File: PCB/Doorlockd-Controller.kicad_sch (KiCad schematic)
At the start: 58 parts, among them J10 Power Out 1, J11 DC in, J12 GPIO 3, J13 Debug UART, J14 GPIO 4, J15 Power Out 2, J16 to extra screw conn., J18 GPIO only MilkV 1.8V, J19 3V 5V Vin, J20 3V 5V Vin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

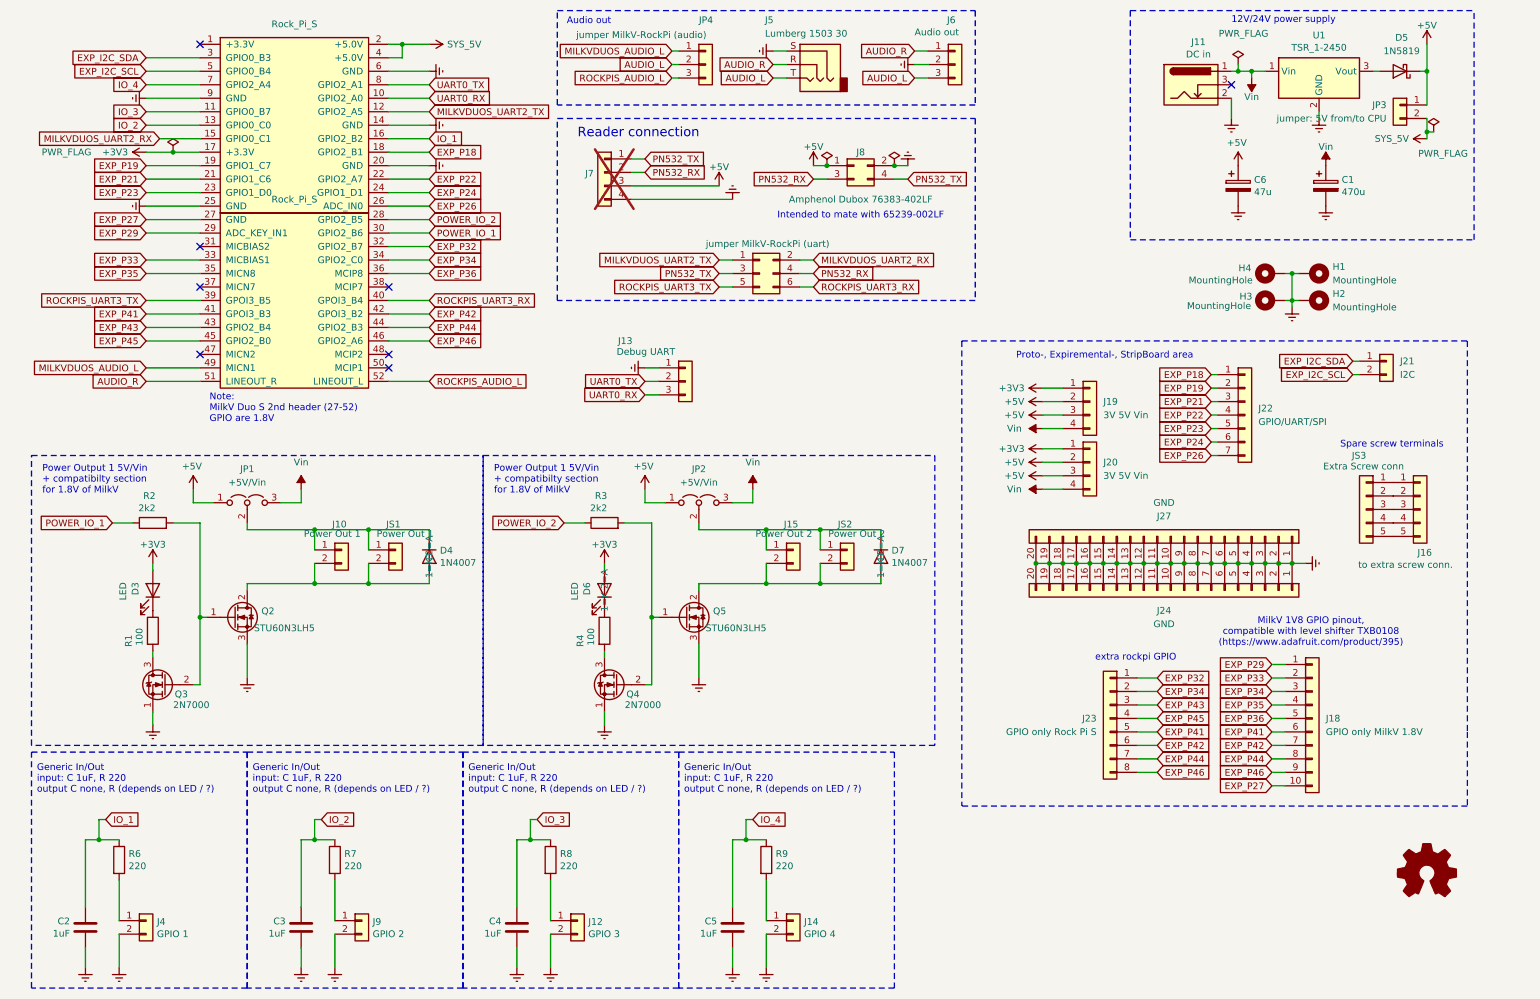
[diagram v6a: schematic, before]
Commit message: Fixed and improved spreadsheet, pcb and schema
PCB and Schema:
improved netlabels for PN532 related pins.
improved netlabels for OUT_1 / OUT_2
improved netlabels for EXP P03 / EXP P05 , and fixed copper lines accoording to silkscreen labels.
added 3.3V pin on PCB intended for lelvel shifter Milk V DUO S (EXP_P43)
Added help lines for mountingholes on fab layer.
Fixed mounting holes for 120x90 & 118x91 including correct positioning.

Spreadsheet:
Fixed and improved color and text labels.
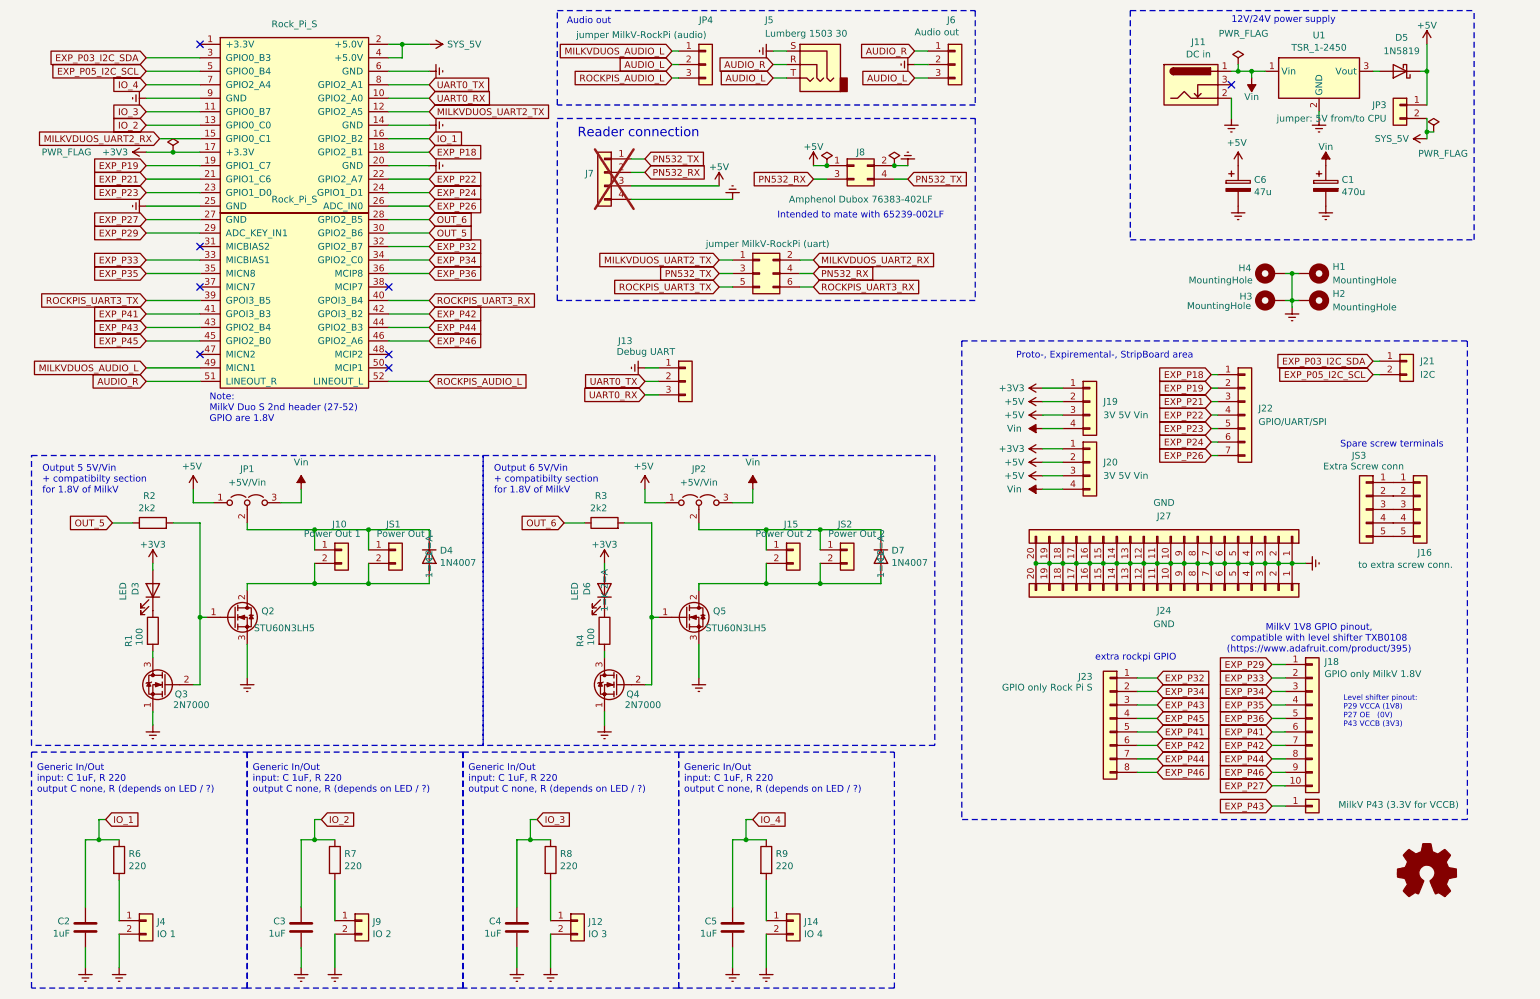
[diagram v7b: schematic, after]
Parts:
- added J1: MilkV P43 (3.3V for VCCB), StripBoard:StripBoard_1x01_P2.54mm, symbol Connector_Generic:Conn_01x01
- H1: footprint MountingHole_3.2x4.32mm_Oval_22.5deg:MountingHole_3.2x4.32mm_Oval_22.5deg_Rtop -> MountingHole_3.2x4.32mm_Oval_22.5deg:MountingHole_3.2x4.32mm_Oval_22.5deg
- H2: footprint MountingHole_3.2x4.32mm_Oval_22.5deg:MountingHole_3.2x4.32mm_Oval_22.5deg_Rbottom -> MountingHole_3.2x4.32mm_Oval_22.5deg:MountingHole_3.2x4.32mm_Oval_22.5deg
- H3: footprint MountingHole_3.2x4.32mm_Oval_22.5deg:MountingHole_3.2x4.32mm_Oval_22.5deg_Lbottom -> MountingHole_3.2x4.32mm_Oval_22.5deg:MountingHole_3.2x4.32mm_Oval_22.5deg
- H4: footprint MountingHole_3.2x4.32mm_Oval_22.5deg:MountingHole_3.2x4.32mm_Oval_22.5deg_Ltop -> MountingHole_3.2x4.32mm_Oval_22.5deg:MountingHole_3.2x4.32mm_Oval_22.5deg
- J12: value GPIO 3 -> IO 3
- J14: value GPIO 4 -> IO 4
- J4: value GPIO 1 -> IO 1
- J9: value GPIO 2 -> IO 2
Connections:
- net EXP_P43: now also J1.1 (Pin_1)
- net EXP_I2C_SCL renamed EXP_P05_I2C_SCL
- net EXP_I2C_SDA renamed EXP_P03_I2C_SDA
- net POWER_IO_1 renamed OUT_5
- net POWER_IO_2 renamed OUT_6
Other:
- note added: "Level shifter pinout: P29 VCCA (1V8) P27 OE (0V) P43 VCCB (3V3)"
- note added: "Output 5 5V/Vin + compatibilty section for 1.8V of MilkV"
- note added: "Output 6 5V/Vin + compatibilty section for 1.8V of MilkV"
- note removed: "Power Output 1 5V/Vin + compatibilty section for 1.8V of MilkV"
- moved on the sheet: J21
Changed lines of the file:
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@@
 		)
 	)
-	(text "Power Output 1 5V/Vin\n+ compatibilty section \nfor 1.8V of MilkV "
+	(text "Output 6 5V/Vin\n+ compatibilty section \nfor 1.8V of MilkV "
 		(exclude_from_sim no)
 		(at 99.822 103.886 0)
@@
 	(text "MilkV 1V8 GPIO pinout, \ncompatible with level shifter TXB0108 \n(https://www.adafruit.com/product/395)"
 		(exclude_from_sim no)
-		(at 253.746 129.794 0)
+		(at 255.27 131.064 0)
 		(effects
 			(font
@@
 		)
 	)
-	(text "Power Output 1 5V/Vin\n+ compatibilty section \nfor 1.8V of MilkV "
+	(text "Output 5 5V/Vin\n+ compatibilty section \nfor 1.8V of MilkV "
 		(exclude_from_sim no)
 		(at 14.732 103.886 0)
@@
 		)
 	)
+	(text "Level shifter pinout:\nP29 VCCA (1V8)\nP27 OE   (0V)\nP43 VCCB (3V3)"
+		(exclude_from_sim no)
+		(at 259.842 144.78 0)
+		(effects
+			(font
+				(size 1.016 1.016)
+			)
+			(justify left)
+		)
+	)
 	(text "Proto-, Expiremental-, StripBoard area\n"
 		(exclude_from_sim no)
@@
 	(polyline
 		(pts
-			(xy 283.21 162.56) (xy 187.96 162.56)
+			(xy 283.21 165.1) (xy 187.96 165.1)
 		)
 		(stroke
@@
 	(wire
 		(pts
-			(xy 261.62 81.28) (xy 262.89 81.28)
+			(xy 265.43 81.28) (xy 266.7 81.28)
 		)
 		(stroke
@@
 	(polyline
 		(pts
-			(xy 283.21 148.59) (xy 283.21 162.56)
+			(xy 283.21 148.59) (xy 283.21 165.1)
 		)
 		(stroke
@@
 	(wire
 		(pts
+			(xy 246.38 162.56) (xy 248.92 162.56)
+		)
+		(stroke
+			(width 0)
+			(type default)
+		)
+	)
+	(wire
+		(pts
 			(xy 132.08 105.41) (xy 128.27 105.41)
 		)
@@
 	(wire
 		(pts
-			(xy 261.62 78.74) (xy 262.89 78.74)
+			(xy 265.43 78.74) (xy 266.7 78.74)
 		)
 		(stroke
@@
 	(polyline
 		(pts
-			(xy 187.96 74.93) (xy 187.96 162.56)
+			(xy 187.96 74.93) (xy 187.96 165.1)
 		)
 		(stroke
@@
 		)
 	)
-	(global_label "POWER_IO_1"
+	(global_label "OUT_5"
 		(shape input)
 		(at 87.63 54.61 0)
@@
 		)
 		(property "Intersheetrefs" "${INTERSHEET_REFS}"
-			(at 101.5119 54.61 0)
+			(at 95.7667 54.61 0)
 			(effects
 				(font
@@
 		)
 	)
-	(global_label "EXP_I2C_SCL"
+	(global_label "EXP_P43"
+		(shape input)
+		(at 246.38 162.56 180)
+		(fields_autoplaced yes)
+		(effects
+			(font
+				(size 1.27 1.27)
+			)
+			(justify right)
+		)
+		(property "Intersheetrefs" "${INTERSHEET_REFS}"
+			(at 235.7639 162.56 0)
+			(effects
+				(font
+					(size 1.27 1.27)
+				)
+				(justify right)
+				(hide yes)
+			)
+		)
+	)
+	(global_label "EXP_P05_I2C_SCL"
 		(shape input)
 		(at 34.29 24.13 180)
@@
 		)
 		(property "Intersheetrefs" "${INTERSHEET_REFS}"
-			(at 19.8034 24.13 0)
+			(at 15.1468 24.13 0)
 			(effects
 				(font
@@
 		)
 	)
-	(global_label "EXP_I2C_SDA"
+	(global_label "EXP_P03_I2C_SDA"
 		(shape input)
 		(at 34.29 21.59 180)
@@
 		)
 		(property "Intersheetrefs" "${INTERSHEET_REFS}"
-			(at 19.7429 21.59 0)
+			(at 15.0863 21.59 0)
 			(effects
 				(font
@@
 		)
 	)
-	(global_label "POWER_IO_1"
+	(global_label "OUT_5"
 		(shape input)
 		(at 27.94 109.22 180)
@@
 		)
 		(property "Intersheetrefs" "${INTERSHEET_REFS}"
-			(at 14.0581 109.22 0)
+			(at 19.8033 109.22 0)
 			(effects
 				(font
@@
 		)
 	)
-	(global_label "POWER_IO_2"
+	(global_label "OUT_6"
 		(shape input)
 		(at 87.63 52.07 0)
@@
 		)
 		(property "Intersheetrefs" "${INTERSHEET_REFS}"
-			(at 101.5119 52.07 0)
+			(at 95.7667 52.07 0)
 			(effects
 				(font
@@
 		)
 	)
-	(global_label "EXP_I2C_SDA"
+	(global_label "EXP_P03_I2C_SDA"
 		(shape input)
-		(at 261.62 78.74 180)
+		(at 265.43 78.74 180)
 		(fields_autoplaced yes)
 		(effects
@@
 		)
 		(property "Intersheetrefs" "${INTERSHEET_REFS}"
-			(at 247.0729 78.74 0)
+			(at 246.2263 78.74 0)
 			(effects
 				(font
@@
 		)
 	)
-	(global_label "EXP_I2C_SCL"
+	(global_label "EXP_P05_I2C_SCL"
 		(shape input)
-		(at 261.62 81.28 180)
+		(at 265.43 81.28 180)
 		(fields_autoplaced yes)
 		(effects
@@
 		)
 		(property "Intersheetrefs" "${INTERSHEET_REFS}"
-			(at 247.1334 81.28 0)
+			(at 246.2868 81.28 0)
 			(effects
 				(font
@@
 		)
 	)
-	(global_label "POWER_IO_2"
+	(global_label "OUT_6"
 		(shape input)
 		(at 113.03 109.22 180)
@@
 		)
 		(property "Intersheetrefs" "${INTERSHEET_REFS}"
-			(at 99.1481 109.22 0)
+			(at 104.8933 109.22 0)
 			(effects
 				(font
@@
 			)
 		)
-		(property "Value" "GPIO 1"
+		(property "Value" "IO 1"
 			(at 36.322 186.6646 0)
 			(effects
@@
 			)
 		)
-		(property "Footprint" "MountingHole_3.2x4.32mm_Oval_22.5deg:MountingHole_3.2x4.32mm_Oval_22.5deg_Rbottom"
+		(property "Footprint" "MountingHole_3.2x4.32mm_Oval_22.5deg:MountingHole_3.2x4.32mm_Oval_22.5deg"
 			(at 254 67.31 0)
 			(effects
@@
 	(symbol
 		(lib_id "Connector_Generic:Conn_01x02")
-		(at 267.97 78.74 0)
+		(at 271.78 78.74 0)
 		(unit 1)
 		(exclude_from_sim no)
@@
 		(fields_autoplaced yes)
 		(property "Reference" "J21"
-			(at 270.51 78.7399 0)
+			(at 274.32 78.7399 0)
 			(effects
 				(font
@@
 		)
 		(property "Value" "I2C"
-			(at 270.51 81.2799 0)
+			(at 274.32 81.2799 0)
 			(effects
 				(font
@@
 		)
 		(property "Footprint" "StripBoard:StripBoard_1x02_P2.54mm"
-			(at 267.97 78.74 0)
+			(at 271.78 78.74 0)
 			(effects
 				(font
@@
 		)
 		(property "Datasheet" "~"
-			(at 267.97 78.74 0)
+			(at 271.78 78.74 0)
 			(effects
 				(font
@@
 		)
 		(property "Description" "Generic connector, single row, 01x02, script generated (kicad-library-utils/schlib/autogen/connector/)"
-			(at 267.97 78.74 0)
+			(at 271.78 78.74 0)
 			(effects
 				(font
@@
 			)
 		)
-		(property "Footprint" "MountingHole_3.2x4.32mm_Oval_22.5deg:MountingHole_3.2x4.32mm_Oval_22.5deg_Lbottom"
+		(property "Footprint" "MountingHole_3.2x4.32mm_Oval_22.5deg:MountingHole_3.2x4.32mm_Oval_22.5deg"
 			(at 246.38 67.31 0)
 			(effects
@@
 			)
 		)
-		(property "Footprint" "MountingHole_3.2x4.32mm_Oval_22.5deg:MountingHole_3.2x4.32mm_Oval_22.5deg_Ltop"
+		(property "Footprint" "MountingHole_3.2x4.32mm_Oval_22.5deg:MountingHole_3.2x4.32mm_Oval_22.5deg"
 			(at 246.38 62.23 0)
 			(effects
@@
 		(dnp no)
 		(property "Reference" "J23"
-			(at 213.36 146.0499 0)
+			(at 212.598 138.176 0)
 			(effects
 				(font
@@
 		)
 		(property "Value" "GPIO only Rock Pi S"
-			(at 213.36 148.5899 0)
+			(at 212.598 140.208 0)
 			(effects
 				(font
@@
 		(dnp no)
 		(property "Reference" "J18"
-			(at 256.54 146.0499 0)
+			(at 256.286 135.382 0)
 			(effects
 				(font
@@
 		)
 		(property "Value" "GPIO only MilkV 1.8V"
-			(at 256.54 148.5899 0)
+			(at 256.286 137.668 0)
 			(effects
 				(font
@@
 			)
 		)
-		(property "Value" "GPIO 3"
+		(property "Value" "IO 3"
 			(at 117.602 186.6646 0)
 			(effects
@@
 			)
 		)
-		(property "Value" "GPIO 2"
+		(property "Value" "IO 2"
 			(at 76.962 186.6646 0)
 			(effects
@@
 	)
 	(symbol
+		(lib_id "Connector_Generic:Conn_01x01")
+		(at 254 162.56 0)
+		(unit 1)
+		(exclude_from_sim no)
+		(in_bom yes)
+		(on_board yes)
+		(dnp no)
+		(property "Reference" "J1"
+			(at 254 168.91 0)
+			(effects
+				(font
+					(size 1.27 1.27)
+				)
+				(hide yes)
+			)
+		)
+		(property "Value" "MilkV P43 (3.3V for VCCB)"
+			(at 270.256 162.306 0)
+			(effects
+				(font
+					(size 1.27 1.27)
+				)
+			)
+		)
+		(property "Footprint" "StripBoard:StripBoard_1x01_P2.54mm"
+			(at 254 162.56 0)
+			(effects
+				(font
+					(size 1.27 1.27)
+				)
+				(hide yes)
+			)
+		)
+		(property "Datasheet" "~"
+			(at 254 162.56 0)
+			(effects
+				(font
+					(size 1.27 1.27)
+				)
+				(hide yes)
+			)
+		)
+		(property "Description" "Generic connector, single row, 01x01, script generated (kicad-library-utils/schlib/autogen/connector/)"
+			(at 254 162.56 0)
+			(effects
+				(font
+					(size 1.27 1.27)
+				)
+				(hide yes)
+			)
+		)
+		(pin "1"
+		)
+		(instances
+			(project ""
+				(path "/dc6b37fb-2353-4b5c-a157-7d8097df64c7"
+					(reference "J1")
+					(unit 1)
+				)
+			)
+		)
+	)
+	(symbol
 		(lib_id "Mechanical:MountingHole_Pad")
 		(at 254 62.23 270)
@@
 			)
 		)
-		(property "Footprint" "MountingHole_3.2x4.32mm_Oval_22.5deg:MountingHole_3.2x4.32mm_Oval_22.5deg_Rtop"
+		(property "Footprint" "MountingHole_3.2x4.32mm_Oval_22.5deg:MountingHole_3.2x4.32mm_Oval_22.5deg"
 			(at 254 62.23 0)
 			(effects
@@
 			)
 		)
-		(property "Value" "GPIO 4"
+		(property "Value" "IO 4"
 			(at 158.242 186.6646 0)
 			(effects

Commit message: Cosmetic schematic changes
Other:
- note added: "FET for 1.8V Milk-V outputs"
- note added: "Level shifter pinout: P29 VCCA (1V8 from GPIO) P27 OE (0V) P43 VCCB (3V3)"
- note added: "Output 5 5V/Vin"
- note added: "Output 6 5V/Vin"
- note added: "Proto-, Experimental-, StripBoard area"
- note removed: "Level shifter pinout: P29 VCCA (1V8) P27 OE (0V) P43 VCCB (3V3)"
- note removed: "Output 5 5V/Vin + compatibilty section for 1.8V of MilkV"
- note removed: "Output 6 5V/Vin + compatibilty section for 1.8V of MilkV"
- note removed: "Proto-, Expiremental-, StripBoard area"
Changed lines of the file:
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@@
 		)
 	)
-	(text "Output 6 5V/Vin\n+ compatibilty section \nfor 1.8V of MilkV "
+	(text "Output 6 5V/Vin"
 		(exclude_from_sim no)
-		(at 99.822 103.886 0)
+		(at 99.06 100.33 0)
 		(effects
 			(font
@@
 		)
 	)
+	(text "FET for 1.8V\nMilk-V outputs"
+		(exclude_from_sim no)
+		(at 25.4 143.51 0)
+		(effects
+			(font
+				(size 1.27 1.27)
+			)
+		)
+	)
 	(text "MilkV 1V8 GPIO pinout, \ncompatible with level shifter TXB0108 \n(https://www.adafruit.com/product/395)"
 		(exclude_from_sim no)
@@
 		)
 	)
-	(text "Output 5 5V/Vin\n+ compatibilty section \nfor 1.8V of MilkV "
+	(text "Output 5 5V/Vin"
 		(exclude_from_sim no)
-		(at 14.732 103.886 0)
+		(at 13.97 100.33 0)
 		(effects
 			(font
@@
 		)
 	)
-	(text "Level shifter pinout:\nP29 VCCA (1V8)\nP27 OE   (0V)\nP43 VCCB (3V3)"
+	(text "Level shifter pinout:\nP29 VCCA (1V8 from GPIO)\nP27 OE   (0V)\nP43 VCCB (3V3)"
 		(exclude_from_sim no)
 		(at 259.842 144.78 0)
@@
 		)
 	)
-	(text "Proto-, Expiremental-, StripBoard area\n"
+	(text "Proto-, Experimental-, StripBoard area\n"
 		(exclude_from_sim no)
 		(at 214.884 77.724 0)
@@
 		)
 	)
+	(text "FET for 1.8V\nMilk-V outputs"
+		(exclude_from_sim no)
+		(at 110.49 143.51 0)
+		(effects
+			(font
+				(size 1.27 1.27)
+			)
+		)
+	)
 	(text "Generic In/Out \ninput: C 1uF, R 220\noutput C none, R (depends on LED / ?)"
 		(exclude_from_sim no)
@@
 		(dnp no)
 		(property "Reference" "JS3"
-			(at 264.16 96.52 0)
+			(at 265.43 115.57 0)
 			(effects
 				(font
@@
 				)
 				(justify left)
+				(hide yes)
 			)
 		)
@@
 		(at 53.34 105.41 0)
 		(unit 1)
-		(exclude_from_sim yes)
+		(exclude_from_sim no)
 		(in_bom no)
 		(on_board yes)
@@
 		(at 138.43 105.41 0)
 		(unit 1)
-		(exclude_from_sim yes)
+		(exclude_from_sim no)
 		(in_bom no)
 		(on_board yes)
@@
 		)
 		(property "Value" "MilkV P43 (3.3V for VCCB)"
-			(at 270.256 162.306 0)
+			(at 256.54 162.56 0)
 			(effects
 				(font
 					(size 1.27 1.27)
 				)
+				(justify left)
 			)
 		)
@@
 		(dnp no)
 		(property "Reference" "J16"
-			(at 273.812 114.808 0)
+			(at 273.05 115.57 0)
 			(effects
 				(font
@@
 				)
 				(justify left)
+				(hide yes)
 			)
 		)
